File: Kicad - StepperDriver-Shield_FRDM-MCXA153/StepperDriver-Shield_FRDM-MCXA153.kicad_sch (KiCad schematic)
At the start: 18 parts, among them J1 Conn_01x02_Socket, J2 ${ALTIUM_VALUE}, J22 Conn_01x02_Socket, J3 ${ALTIUM_VALUE}, J4 ${ALTIUM_VALUE}, J5 ${ALTIUM_VALUE}, SW1 Home, SW2 SW1, SW3 SW2

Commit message: Update 3D Models
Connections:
- net P2-12/SCK1: now also J5.12 (Pin_12)
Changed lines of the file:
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@@
+	(wire
+		(pts
+			(xy 148.59 38.1) (xy 168.91 38.1)
+		)
+		(stroke
+			(width 0)
+			(type default)
+		)
+	)
 	(wire
 		(pts

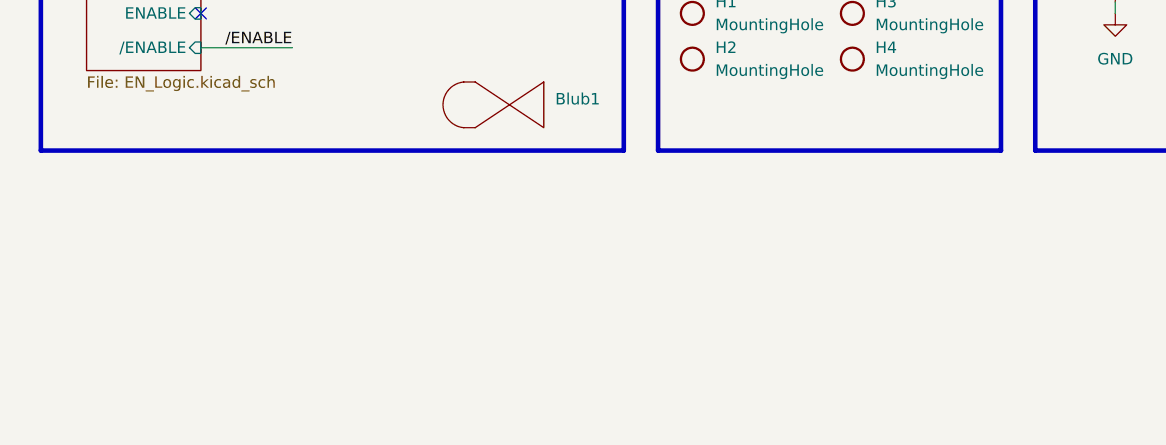
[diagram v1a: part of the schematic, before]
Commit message: Added Status RGB LED
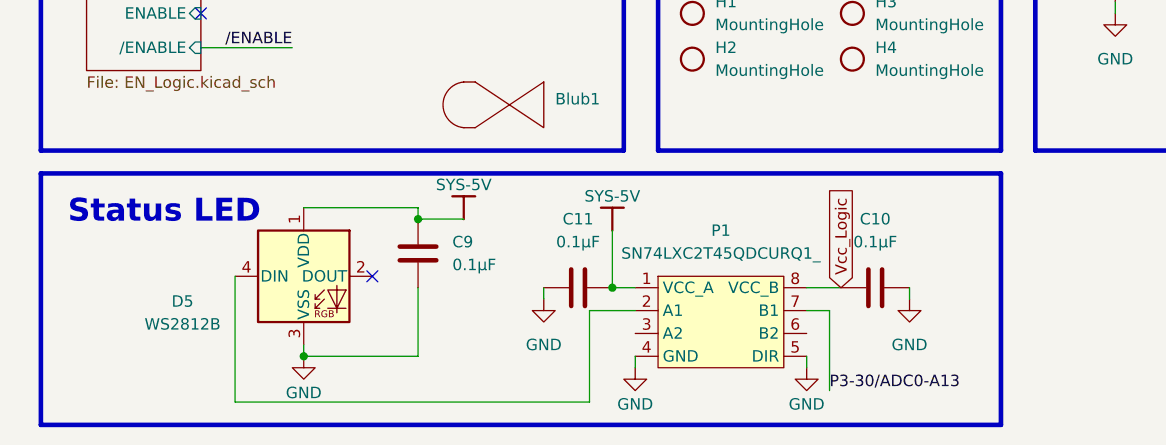
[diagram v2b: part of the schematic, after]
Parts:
- added C10, C11, C9: 0.1µF, Capacitor_SMD:C_0805_2012Metric_Pad1.18x1.45mm_HandSolder, symbol Device:C
- added D5: WS2812B, LED_SMD:LED_WS2812B_PLCC4_5.0x5.0mm_P3.2mm, symbol LED:WS2812B
- added P1: SN74LXC2T45QDCURQ1_, Pegelwandler:SN74LXC2T45QDCURQ1, symbol Pegelwandler:SN74LXC2T45QDCURQ1_
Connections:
- net GND: now also C10.1, C11.2, C9.1, D5.3 (VSS), P1.4 (GND), P1.5 (DIR)
- net LDO-3V3: now also C10.2, P1.8 (VCC_B)
- net P3-30/ADC0-A13: now also P1.7 (B1)
- net SYS-5V: now also C11.1, C9.2, D5.1 (VDD), P1.1 (VCC_A)
- new net: D5.4 (DIN), P1.2 (A1)
- no-connect marks 29 -> 30
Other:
- note added: "Status LED"
